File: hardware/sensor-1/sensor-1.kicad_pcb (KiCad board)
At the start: 2 copper layers, 11 x 155 mm, 15 parts, among them J101 2x05_Horizontal, U101 A31010SEHALT-10, U102 A31010SEHALT-10, U103 A31010SEHALT-10

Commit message: Update sensors
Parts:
- C101, C103, C104: footprint Capacitor_SMD:C_0603_1608Metric -> V2_Capacitor_SMD:C_0603
- FID101, FID102: value Fiducial -> Fiducial_Paste
- INFO101: value ORDER-NUMBER -> Order_Number

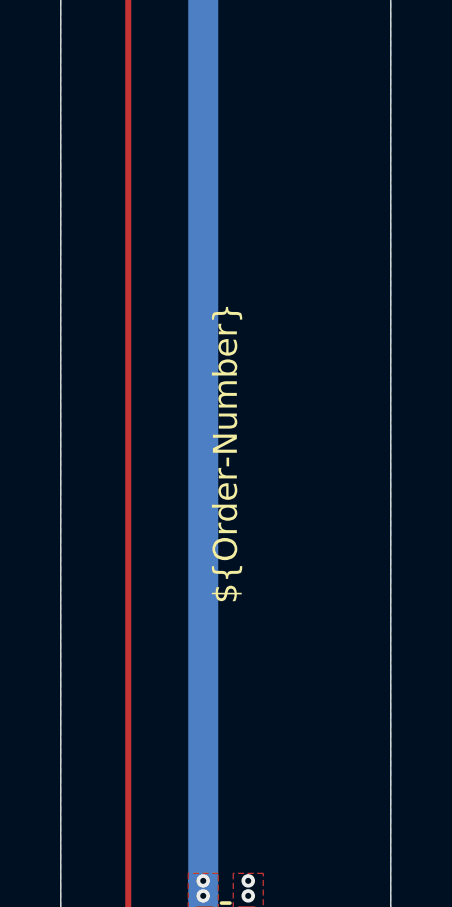
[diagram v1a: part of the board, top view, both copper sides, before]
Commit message: Replace Order_Number
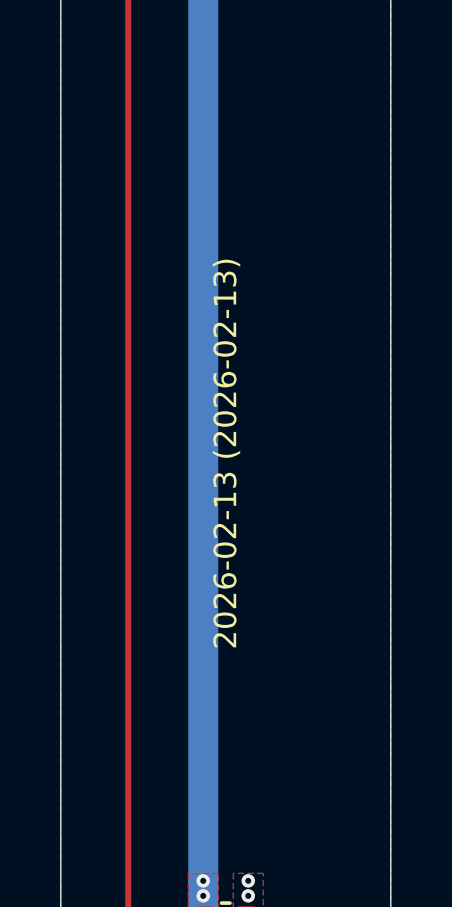
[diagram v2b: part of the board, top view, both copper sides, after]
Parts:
- H107, H108: value MountingHole_2.5mm -> 2.5mm
- INFO101: value Order_Number -> ~; footprint V2_Production:Order_Number -> V2_Production:Revision
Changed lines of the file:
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@@
 	(paper "A4")
 	(title_block
-		(date "2023-07-17")
-		(rev "1")
+		(date "2026-02-13")
+		(rev "2026-02-13")
 	)
 	(layers
@@
 			)
 		)
+		(pad "" smd roundrect
+			(at -0.7 0)
+			(size 0.7 0.8)
+			(layers "F.Paste")
+			(roundrect_rratio 0.1428571429)
+			(chamfer_ratio 0.3)
+			(chamfer top_right bottom_right)
+		)
+		(pad "" smd roundrect
+			(at 0.7 0)
+			(size 0.7 0.8)
+			(layers "F.Paste")
+			(roundrect_rratio 0.1428571429)
+			(chamfer_ratio 0.3)
+			(chamfer top_left bottom_left)
+		)
 		(pad "1" smd roundrect
 			(at -0.7 0)
 			(size 0.7 0.8)
-			(layers "F.Cu" "F.Mask" "F.Paste")
+			(layers "F.Cu" "F.Mask")
 			(roundrect_rratio 0.1428571429)
 			(net 1 "+3V3")
@@
 			(at 0.7 0)
 			(size 0.7 0.8)
-			(layers "F.Cu" "F.Mask" "F.Paste")
+			(layers "F.Cu" "F.Mask")
 			(roundrect_rratio 0.1428571429)
 			(net 4 "GND")
@@
 		)
 		(embedded_fonts no)
-		(model "${KICAD9_3DMODEL_DIR}/Capacitor_SMD.3dshapes/C_0603_1608Metric.step"
+		(model "../../3dmodels/V2_Capacitor_SMD.3dshapes/C_0603_1608Metric.step"
 			(offset
 				(xyz 0 0 0)
@@
 		)
 		(embedded_fonts no)
-		(model "/Users/kay/Documents/KiCad/8.0/versioduo.kicad/3dmodels/V2_Sensor_Hall.3dshapes/A31010SEHALT-10.stp"
+		(model "../../3dmodels/V2_Sensor_Hall.3dshapes/A31010SEHALT-10.stp"
 			(offset
 				(xyz 0 0 0)
@@
 			)
 		)
-		(property "Value" "MountingHole_2.5mm"
+		(property "Value" "2.5mm"
 			(at 0 2.23 0)
 			(unlocked yes)
@@
 			)
 		)
+		(pad "" smd roundrect
+			(at -0.7 0)
+			(size 0.7 0.8)
+			(layers "F.Paste")
+			(roundrect_rratio 0.1428571429)
+			(chamfer_ratio 0.3)
+			(chamfer top_right bottom_right)
+		)
+		(pad "" smd roundrect
+			(at 0.7 0)
+			(size 0.7 0.8)
+			(layers "F.Paste")
+			(roundrect_rratio 0.1428571429)
+			(chamfer_ratio 0.3)
+			(chamfer top_left bottom_left)
+		)
 		(pad "1" smd roundrect
 			(at -0.7 0)
 			(size 0.7 0.8)
-			(layers "F.Cu" "F.Mask" "F.Paste")
+			(layers "F.Cu" "F.Mask")
 			(roundrect_rratio 0.1428571429)
 			(net 1 "+3V3")
@@
 			(at 0.7 0)
 			(size 0.7 0.8)
-			(layers "F.Cu" "F.Mask" "F.Paste")
+			(layers "F.Cu" "F.Mask")
 			(roundrect_rratio 0.1428571429)
 			(net 4 "GND")
@@
 		)
 		(embedded_fonts no)
-		(model "${KICAD9_3DMODEL_DIR}/Capacitor_SMD.3dshapes/C_0603_1608Metric.step"
+		(model "../../3dmodels/V2_Capacitor_SMD.3dshapes/C_0603_1608Metric.step"
 			(offset
 				(xyz 0 0 0)
@@
 		)
 		(embedded_fonts no)
-		(model "/Users/kay/Documents/KiCad/8.0/versioduo.kicad/3dmodels/V2_Sensor_Hall.3dshapes/A31010SEHALT-10.stp"
+		(model "../../3dmodels/V2_Sensor_Hall.3dshapes/A31010SEHALT-10.stp"
 			(offset
 				(xyz 0 0 0)
@@
 		(embedded_fonts no)
 	)
-	(footprint "V2_Production:Order_Number"
+	(footprint "V2_Production:Revision"
 		(layer "F.Cu")
 		(at 159.75 105 90)
@@
 			)
 		)
-		(property "Value" "Order_Number"
+		(property "Value" "~"
 			(at 0 2.27 90)
 			(unlocked yes)
@@
 		(sheetname "/")
 		(sheetfile "sensor-1.kicad_sch")
-		(attr exclude_from_pos_files exclude_from_bom)
-		(fp_rect
-			(start -7 -0.75)
-			(end 7 0.75)
-			(stroke
-				(width 0.05)
-				(type default)
-			)
-			(fill no)
-			(layer "F.CrtYd")
-		)
-		(fp_text user "${Order-Number}"
+		(attr exclude_from_pos_files exclude_from_bom allow_missing_courtyard)
+		(fp_text user "${REVISION} (${ISSUE_DATE})"
 			(at 0 0 90)
 			(unlocked yes)
@@
 			(effects
 				(font
-					(size 0.8 0.8)
-					(thickness 0.12)
+					(size 0.75 0.75)
+					(thickness 0.1)
+				)
+			)
+		)
+		(fp_text user "${REVISION} (${ISSUE_DATE})"
+			(at 0 0 90)
+			(unlocked yes)
+			(layer "F.Fab")
+			(effects
+				(font
+					(size 0.75 0.75)
+					(thickness 0.1)
 				)
 			)
@@
 		)
 		(embedded_fonts no)
-		(model "/Users/kay/Documents/KiCad/8.0/versioduo.kicad/3dmodels/V2_Sensor_Hall.3dshapes/A31010SEHALT-10.stp"
+		(model "../../3dmodels/V2_Sensor_Hall.3dshapes/A31010SEHALT-10.stp"
 			(offset
 				(xyz 0 0 0)
@@
 			)
 		)
-		(property "Value" "MountingHole_2.5mm"
+		(property "Value" "2.5mm"
 			(at 0 2.23 0)
 			(unlocked yes)
@@
 			)
 		)
+		(pad "" smd roundrect
+			(at -0.7 0)
+			(size 0.7 0.8)
+			(layers "F.Paste")
+			(roundrect_rratio 0.1428571429)
+			(chamfer_ratio 0.3)
+			(chamfer top_right bottom_right)
+		)
+		(pad "" smd roundrect
+			(at 0.7 0)
+			(size 0.7 0.8)
+			(layers "F.Paste")
+			(roundrect_rratio 0.1428571429)
+			(chamfer_ratio 0.3)
+			(chamfer top_left bottom_left)
+		)
 		(pad "1" smd roundrect
 			(at -0.7 0)
 			(size 0.7 0.8)
-			(layers "F.Cu" "F.Mask" "F.Paste")
+			(layers "F.Cu" "F.Mask")
 			(roundrect_rratio 0.1428571429)
 			(net 1 "+3V3")
@@
 			(at 0.7 0)
 			(size 0.7 0.8)
-			(layers "F.Cu" "F.Mask" "F.Paste")
+			(layers "F.Cu" "F.Mask")
 			(roundrect_rratio 0.1428571429)
 			(net 4 "GND")
@@
 		)
 		(embedded_fonts no)
-		(model "${KICAD9_3DMODEL_DIR}/Capacitor_SMD.3dshapes/C_0603_1608Metric.step"
+		(model "../../3dmodels/V2_Capacitor_SMD.3dshapes/C_0603_1608Metric.step"
 			(offset
 				(xyz 0 0 0)

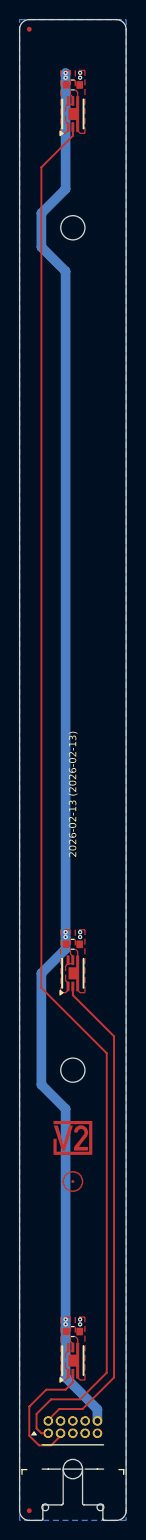
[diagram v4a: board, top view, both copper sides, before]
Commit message: KiCad 10
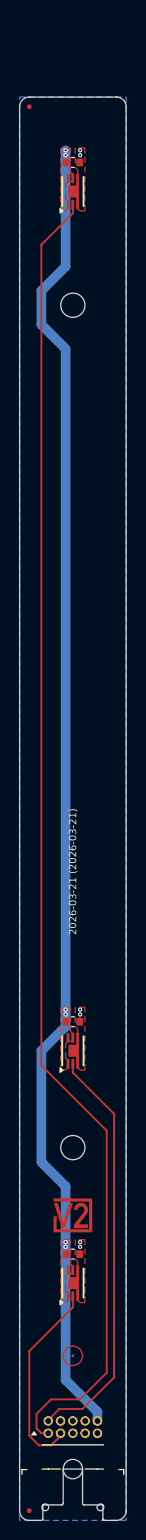
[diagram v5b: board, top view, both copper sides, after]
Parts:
- moved ICON102 18.0 mm to (159.8, 163.0)
- moved C101 8.00 mm to (159.8, 39.8)
- moved C103 8.00 mm to (159.8, 152.5)
- moved C104 8.00 mm to (159.8, 128.5)
- moved FID102 8.00 mm to (155.2, 34.0)
- moved H107 8.00 mm to (159.8, 54.5)
- moved H108 8.00 mm to (159.8, 141.5)
- moved ICON101 8.00 mm to (159.8, 148.5)
- moved INFO101 8.00 mm to (159.8, 113.0)
- moved U101 8.00 mm to (159.8, 42.8)
- moved U102 8.00 mm to (159.8, 131.5)
- moved U103 8.00 mm to (159.8, 155.5)
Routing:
- net /Sensor-2: track 50.9 -> 42.9 mm
- net /Sensor-1: track 145.0 -> 137.0 mm
- net +3V3: track 144.7 -> 136.7 mm
- net /Sensor-3: track 13.4 -> 20.6 mm
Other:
- board size 11 x 155 mm -> 11 x 147 mm
